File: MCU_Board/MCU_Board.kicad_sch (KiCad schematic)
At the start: 0 parts

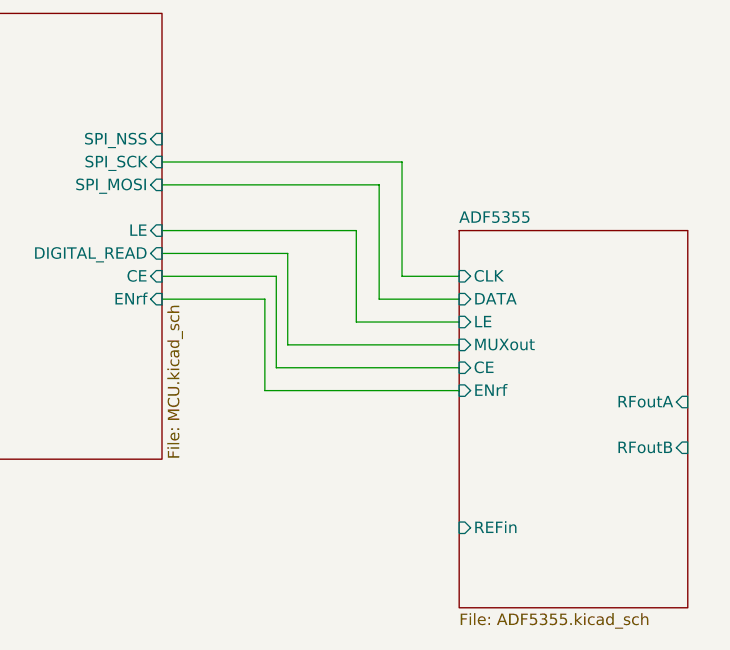
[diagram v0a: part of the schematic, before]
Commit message: Split the project in two
Split the main project in two parts
One is the MCU part and the second is VCO
This was made for the purpose of designing two PCB boards.
In case the MCU part is not designed properly, it can be remade on a cheaper material than the VCO board.
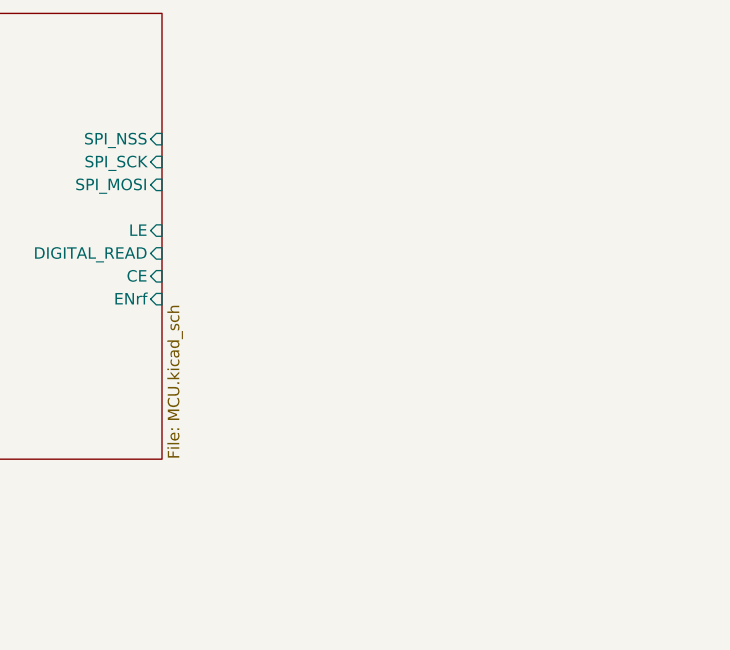
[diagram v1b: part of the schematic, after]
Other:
- removed sheet ADF5355
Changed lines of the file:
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@@
-    (stroke (width 0) (type default))
-  )
-  (wire (pts (xy 193.04 78.74) (xy 204.47 78.74))
     (stroke (width 0) (type default))
   )
@@
     (stroke (width 0) (type default))
   )
-  (wire (pts (xy 185.42 81.28) (xy 204.47 81.28))
-    (stroke (width 0) (type default))
-  )
   (wire (pts (xy 115.57 78.74) (xy 115.57 96.52))
-    (stroke (width 0) (type default))
-  )
-  (wire (pts (xy 182.88 76.2) (xy 182.88 86.36))
     (stroke (width 0) (type default))
   )
@@
     (stroke (width 0) (type default))
   )
-  (wire (pts (xy 195.58 63.5) (xy 195.58 76.2))
-    (stroke (width 0) (type default))
-  )
   (wire (pts (xy 64.77 58.42) (xy 128.27 58.42))
-    (stroke (width 0) (type default))
-  )
-  (wire (pts (xy 184.15 73.66) (xy 184.15 83.82))
     (stroke (width 0) (type default))
   )
@@
     (stroke (width 0) (type default))
   )
-  (wire (pts (xy 185.42 71.12) (xy 185.42 81.28))
-    (stroke (width 0) (type default))
-  )
   (wire (pts (xy 67.31 55.88) (xy 128.27 55.88))
-    (stroke (width 0) (type default))
-  )
-  (wire (pts (xy 171.45 73.66) (xy 184.15 73.66))
-    (stroke (width 0) (type default))
-  )
-  (wire (pts (xy 171.45 71.12) (xy 185.42 71.12))
-    (stroke (width 0) (type default))
-  )
-  (wire (pts (xy 184.15 83.82) (xy 204.47 83.82))
     (stroke (width 0) (type default))
   )
@@
     (stroke (width 0) (type default))
   )
-  (wire (pts (xy 171.45 76.2) (xy 182.88 76.2))
-    (stroke (width 0) (type default))
-  )
   (wire (pts (xy 113.03 76.2) (xy 113.03 93.98))
-    (stroke (width 0) (type default))
-  )
-  (wire (pts (xy 198.12 73.66) (xy 198.12 60.96))
     (stroke (width 0) (type default))
   )
@@
     (stroke (width 0) (type default))
   )
-  (wire (pts (xy 171.45 68.58) (xy 193.04 68.58))
-    (stroke (width 0) (type default))
-  )
   (wire (pts (xy 128.27 78.74) (xy 115.57 78.74))
-    (stroke (width 0) (type default))
-  )
-  (wire (pts (xy 182.88 86.36) (xy 204.47 86.36))
     (stroke (width 0) (type default))
   )
@@
     (stroke (width 0) (type default))
   )
-  (wire (pts (xy 171.45 63.5) (xy 195.58 63.5))
-    (stroke (width 0) (type default))
-  )
-  (wire (pts (xy 195.58 76.2) (xy 204.47 76.2))
-    (stroke (width 0) (type default))
-  )
   (wire (pts (xy 128.27 76.2) (xy 113.03 76.2))
-    (stroke (width 0) (type default))
-  )
-  (wire (pts (xy 198.12 73.66) (xy 204.47 73.66))
     (stroke (width 0) (type default))
   )
@@
     (stroke (width 0) (type default))
   )
-  (wire (pts (xy 193.04 68.58) (xy 193.04 78.74))
-    (stroke (width 0) (type default))
-  )
   (bus (pts (xy 66.04 99.06) (xy 119.38 99.06))
-    (stroke (width 0) (type default))
-  )
-  (wire (pts (xy 171.45 60.96) (xy 198.12 60.96))
     (stroke (width 0) (type default))
   )
@@
     )
     (instances
-      (project "ADF5355_VCO"
+      (project "MCU_Board"
         (path "/29349b68-071c-451b-9b1e-10b5ef7e12a6" (page "2"))
       )
@@
     )
     (instances
-      (project "ADF5355_VCO"
+      (project "MCU_Board"
         (path "/29349b68-071c-451b-9b1e-10b5ef7e12a6" (page "3"))
       )
@@
     )
     (instances
-      (project "ADF5355_VCO"
+      (project "MCU_Board"
         (path "/29349b68-071c-451b-9b1e-10b5ef7e12a6" (page "4"))
-      )
-    )
-  )
-  (sheet (at 204.47 68.58) (size 25.4 41.91) (fields_autoplaced)
-    (stroke (width 0.1524) (type solid))
-    (fill (color 0 0 0 0.0000))
-    (property "Sheetname" "ADF5355" (at 204.47 67.8684 0)
-      (effects (font (size 1.27 1.27)) (justify left bottom))
-    )
-    (property "Sheetfile" "ADF5355.kicad_sch" (at 204.47 111.0746 0)
-      (effects (font (size 1.27 1.27)) (justify left top))
-    )
-    (pin "ENrf" input (at 204.47 86.36 180)
-      (effects (font (size 1.27 1.27)) (justify left))
-    )
-    (pin "CE" input (at 204.47 83.82 180)
-      (effects (font (size 1.27 1.27)) (justify left))
-    )
-    (pin "MUXout" input (at 204.47 81.28 180)
-      (effects (font (size 1.27 1.27)) (justify left))
-    )
-    (pin "LE" input (at 204.47 78.74 180)
-      (effects (font (size 1.27 1.27)) (justify left))
-    )
-    (pin "DATA" input (at 204.47 76.2 180)
-      (effects (font (size 1.27 1.27)) (justify left))
-    )
-    (pin "CLK" input (at 204.47 73.66 180)
-      (effects (font (size 1.27 1.27)) (justify left))
-    )
-    (pin "REFin" input (at 204.47 101.6 180)
-      (effects (font (size 1.27 1.27)) (justify left))
-    )
-    (pin "RFoutB" input (at 229.87 92.71 0)
-      (effects (font (size 1.27 1.27)) (justify right))
-    )
-    (pin "RFoutA" input (at 229.87 87.63 0)
-      (effects (font (size 1.27 1.27)) (justify right))
-    )
-    (instances
-      (project "ADF5355_VCO"
-        (path "/29349b68-071c-451b-9b1e-10b5ef7e12a6" (page "6"))
       )
     )
@@
     )
     (instances
-      (project "ADF5355_VCO"
+      (project "MCU_Board"
         (path "/29349b68-071c-451b-9b1e-10b5ef7e12a6" (page "5"))
       )

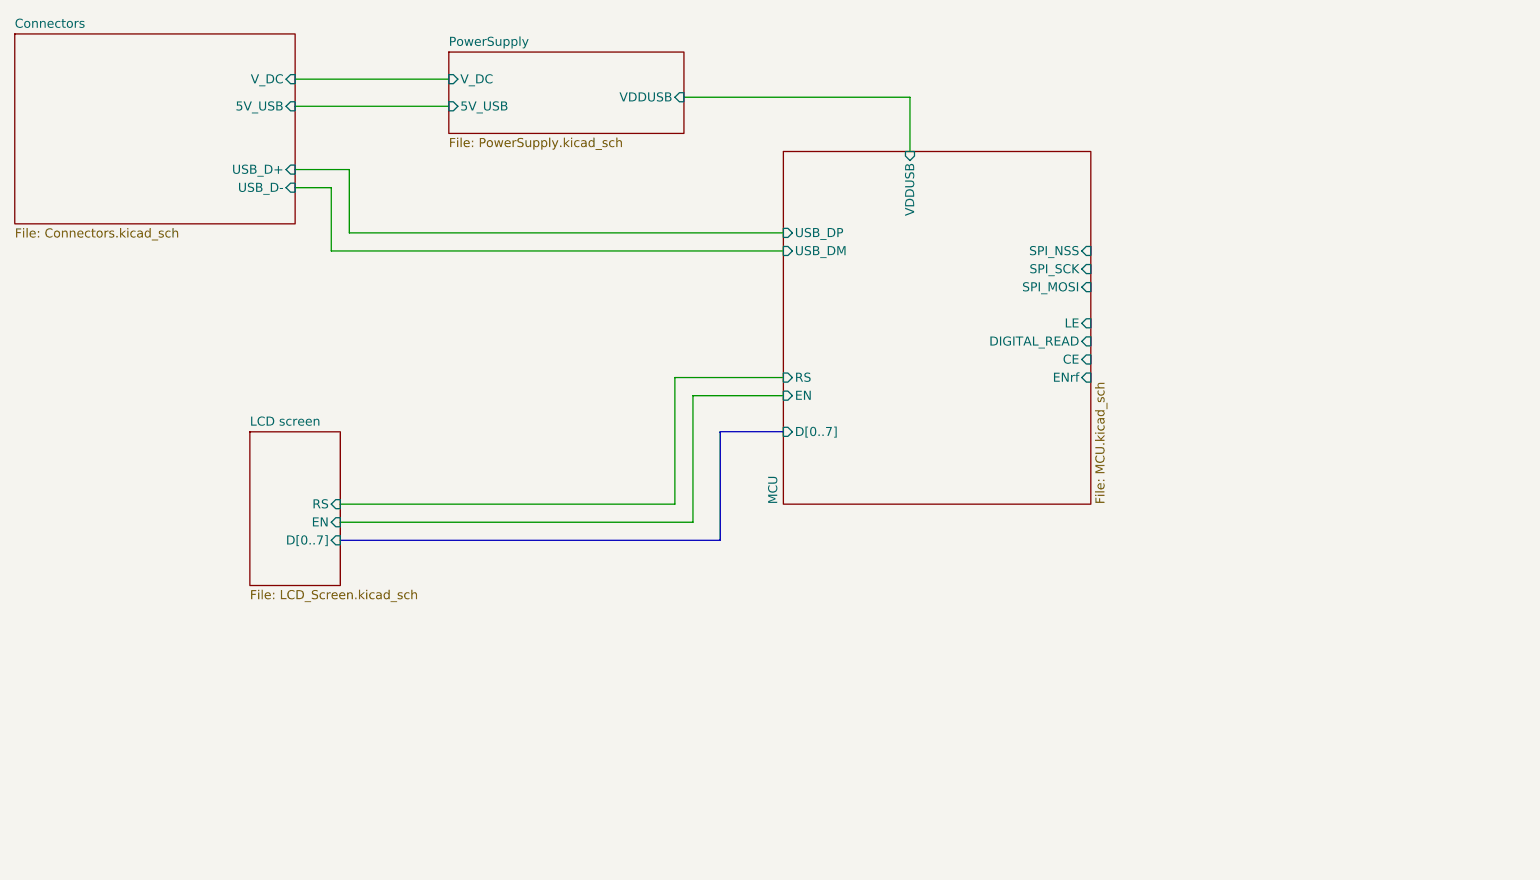
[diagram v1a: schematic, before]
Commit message: Added JTAG connector to MCU board
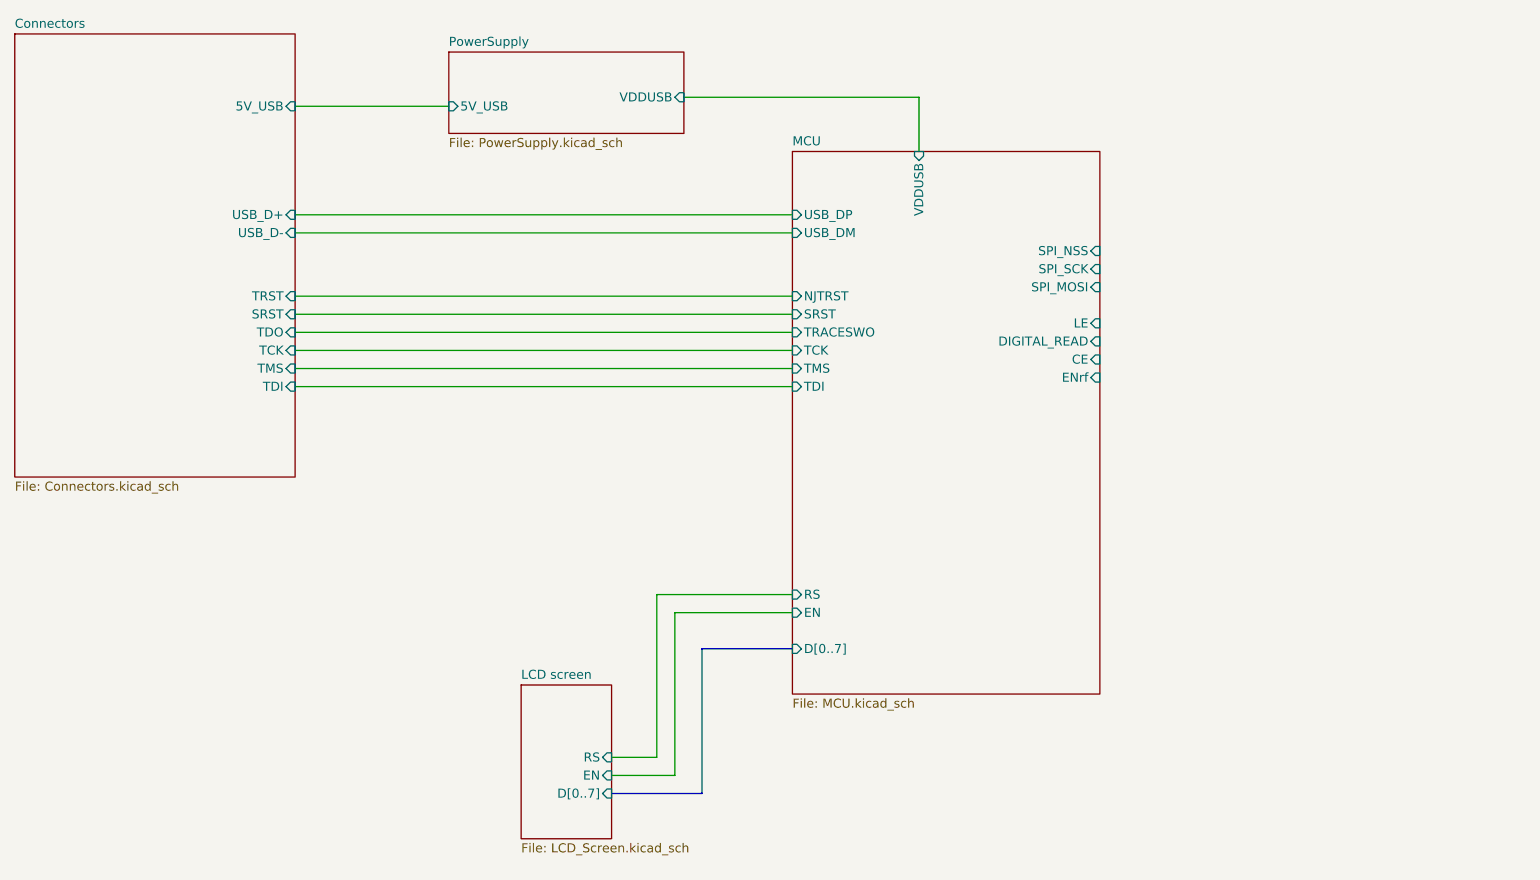
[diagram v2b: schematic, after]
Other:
- sheet Connectors ports: added SRST, TCK, TDI, TDO, TMS, TRST; removed V_DC
- sheet MCU ports: added NJTRST, SRST, TCK, TDI, TMS, TRACESWO; removed none
- sheet PowerSupply ports: added none; removed V_DC
